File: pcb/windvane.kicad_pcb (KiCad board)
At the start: 2 copper layers, 97.5 x 46 mm, 30 parts, among them J1 Screw_Terminal_01x04, J2 Conn_01x04_Pin, U1 ESP-12F, U2 MCP2515-xSO, U3 AS5600-ASOT, U4 DS18B20, U6 TJA1050, Y1 8MHz

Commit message: place & route
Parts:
- removed C3: 0.1u, Capacitor_SMD:C_0805_2012Metric
- removed H1, H2: MountingHole, MountingHole:MountingHole_2.2mm_M2
- removed J1: Screw_Terminal_01x04, TerminalBlock_Phoenix:TerminalBlock_Phoenix_MKDS-1,5-4-5.08_1x04_P5.08mm_Horizontal
- removed J2: Conn_01x04_Pin, Connector_JST:JST_EH_S4B-EH_1x04_P2.50mm_Horizontal
- removed R3: 10k, Resistor_SMD:R_0805_2012Metric
- removed SS40AF1: ~, Package_TO_SOT_THT:TO-92L_Inline
- added C8: 10u, Capacitor_SMD:C_0805_2012Metric, F.Cu at (139.1, 96.0)
- added J3: Conn_01x08_Socket, Connector_FFC-FPC:Molex_200528-0080_1x08-1MP_P1.00mm_Horizontal, F.Cu at (126.8, 118.3)
- added R11: 10k, Resistor_SMD:R_0805_2012Metric, F.Cu at (134.5, 110.0)
- added U5: ~, Custom:MiniStepDownConverter, F.Cu at (126.1, 103.8)
- added U7: SS40AF1, Package_TO_SOT_THT:TO-92L_Inline, B.Cu at (138.0, 108.6)
- C1, C2: value 22u -> 10u; footprint Capacitor_SMD:C_Elec_5x5.8 -> Capacitor_SMD:C_0805_2012Metric
- C6, C7: value 0.1u -> 10u
- U3: footprint Package_SO:Infineon_PG-DSO-8-43 -> Package_SO:SOIC-8_3.9x4.9mm_P1.27mm
- moved R1 73.3 mm to (159.5, 89.3), turned to -90 degrees
- moved R5 70.6 mm to (155.6, 111.1), turned to 90 degrees
- moved R2 69.4 mm to (155.7, 89.3), turned to -90 degrees
- moved R4 69.3 mm to (153.6, 111.1), turned to 90 degrees
- moved R6 65.9 mm to (151.6, 111.1), turned to 90 degrees
- moved R7 63.0 mm to (149.6, 111.1), turned to 90 degrees
- moved R8 60.1 mm to (147.6, 111.1), turned to -90 degrees
- moved H3 46.2 mm to (153.5, 117.0)
- moved C1 40.8 mm to (134.5, 107.7)
- moved C2 39.3 mm to (145.6, 89.3), turned to -90 degrees
- moved Y1 38.1 mm to (138.5, 90.4), turned to 90 degrees
- moved H4 37.4 mm to (153.7, 85.0)
- moved C4 31.1 mm to (134.5, 86.2), turned to 90 degrees
- moved C5 31.0 mm to (134.5, 89.7), turned to -90 degrees
- moved R10 28.2 mm to (116.9, 87.5)
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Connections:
- C1 pad 1: +12V -> GND
- C1 pad 2: GND -> +12V
- C2 pad 1: +3V3 -> GND
- C2 pad 2: GND -> +3V3
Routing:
- net /MOSI: track 0.00 -> 41.7 mm, vias 0 -> 2
- net Net-(U2-~{RESET}): track 0.00 -> 7.06 mm
- net +3V3: track 0.00 -> 6.25 mm
- net /Speed_Out: track 0.00 -> 5.07 mm
- net Net-(U2-OSC2): track 0.00 -> 4.16 mm
- net Net-(U2-OSC1): track 0.00 -> 4.11 mm
- net +12V: track 0.00 -> 2.96 mm
- net Net-(U1-~{RST}): track 0.00 -> 2.49 mm
- net Net-(U1-EN): track 0.00 -> 2.48 mm
- net /Temp_DQ: track 0.00 -> 2.46 mm
- net Net-(U1-GPIO2): track 0.00 -> 2.34 mm
- net /uC_PRG: track 0.00 -> 2.34 mm
- net /SDA: track 0.00 -> 2.34 mm
- net /SCL: track 0.00 -> 2.34 mm
- net Net-(U1-GPIO15): track 0.00 -> 2.33 mm
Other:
- board size 97.5 x 46 mm -> 60.8 x 40.8 mm

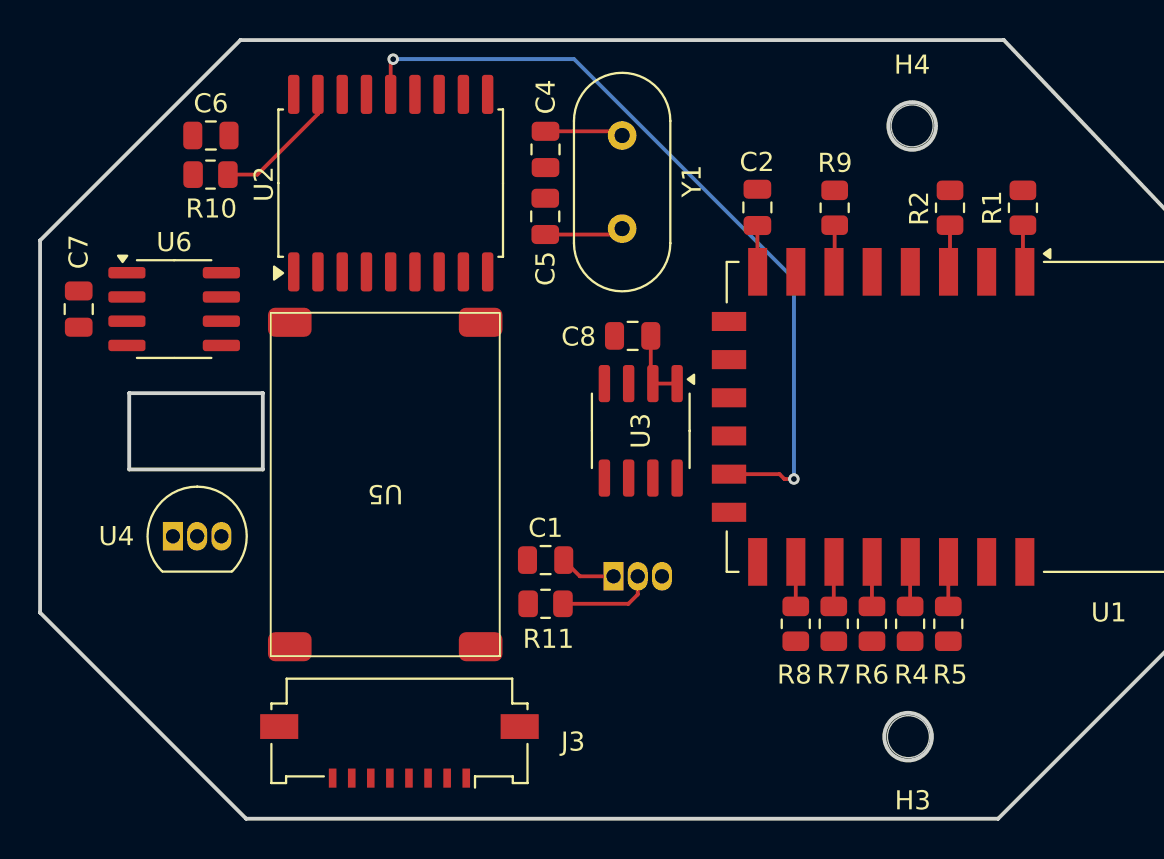
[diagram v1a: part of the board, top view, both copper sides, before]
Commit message: routing - done, next up - review
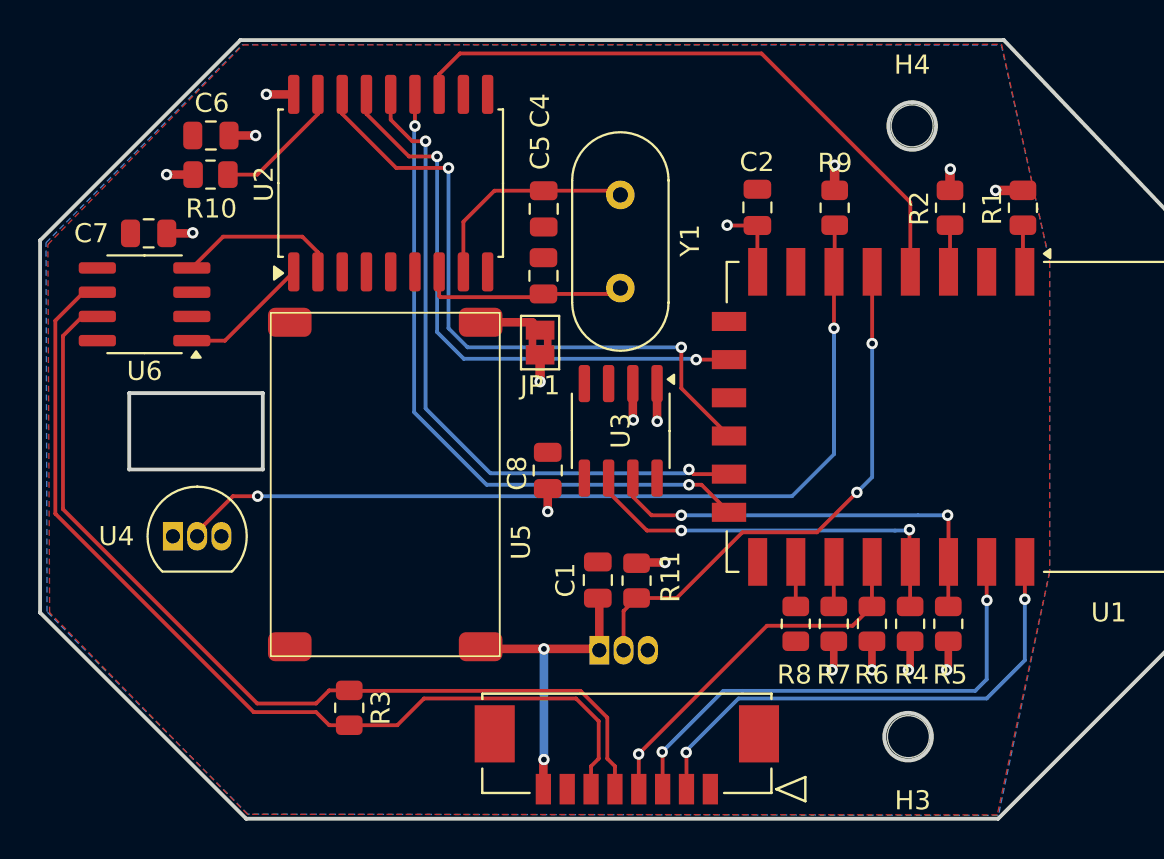
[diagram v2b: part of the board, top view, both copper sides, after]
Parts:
- added JP1: SolderJumper_2_Bridged, Jumper:SolderJumper-2_P1.3mm_Bridged2Bar_Pad1.0x1.5mm, F.Cu at (134.2, 96.3)
- added R3: 120, Resistor_SMD:R_0805_2012Metric, F.Cu at (124.2, 115.5)
- J3: footprint Connector_FFC-FPC:Molex_200528-0080_1x08-1MP_P1.00mm_Horizontal -> Custom:CON_532610871
- moved J3 16.4 mm to (143.1, 119.8)
- moved C8 8.34 mm to (134.6, 103.0), turned to -90 degrees
- moved C7 5.40 mm to (113.7, 90.6), turned to 0 degrees
- moved R11 4.92 mm to (139.3, 108.8), turned to -90 degrees
- moved U7 3.94 mm to (137.3, 112.5)
- moved C4 3.11 mm to (134.4, 89.3)
- moved C5 3.11 mm to (134.4, 92.9)
- moved Y1 3.11 mm to (138.4, 93.5)
- moved C1 2.93 mm to (137.2, 108.8), turned to -90 degrees
- moved U6 1.57 mm to (113.5, 94.3), turned to 180 degrees
- moved U3 1.05 mm to (138.4, 101.0)
- turned U5 to 0 degrees
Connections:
- J3 pad 2: /uC_RXD -> /uC_TXD
- J3 pad 3: /uC_TXD -> /uC_RXD
- J3 pad 5: /CAN_LOW -> /CAN_+
- J3 pad 6: /CAN_HI -> /CAN_-
- U5 pad 3: +3V3 -> Net-(JP1-A)
- U6 pad 6: /CAN_LOW -> /CAN_-
- U6 pad 7: /CAN_HI -> /CAN_+
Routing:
- net /CAN_-: track 0.00 -> 50.8 mm
- net /CAN_+: track 0.00 -> 48.8 mm
- net /Temp_DQ: track 2.46 -> 47.3 mm, vias 0 -> 2
- net /SCLK: track 0.00 -> 35.3 mm, vias 0 -> 2
- net /~{CS}: track 0.00 -> 34.5 mm, vias 0 -> 2
- net /CAN_~{Int}: track 0.00 -> 33.1 mm
- net /MISO: track 0.00 -> 30.7 mm, vias 0 -> 2
- net /uC_TXD: track 0.00 -> 26.9 mm, vias 0 -> 2
- net /uC_RXD: track 0.00 -> 26.7 mm, vias 0 -> 2
- net /Speed_Out: track 5.07 -> 28.7 mm, vias 0 -> 2
- net +3V3: track 6.25 -> 27.5 mm, vias 0 -> 17
- net /SCL: track 2.34 -> 22.7 mm, vias 0 -> 2
- net /SDA: track 2.34 -> 22.2 mm, vias 0 -> 2
- net /uC_PRG: track 2.34 -> 19.7 mm, vias 0 -> 1
- net +12V: track 2.96 -> 16.6 mm, vias 0 -> 2
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- added copper zone on B.Cu, net +3V3
- added copper zone on F.Cu, net GND

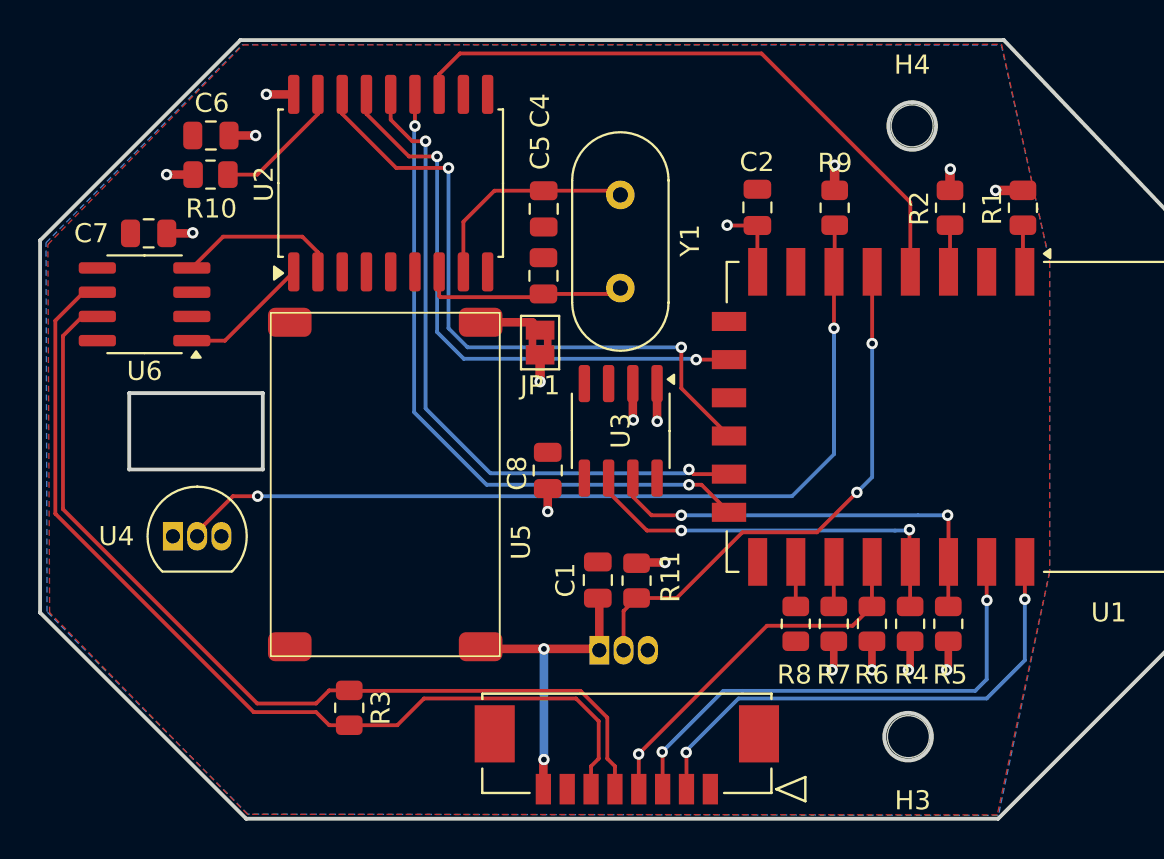
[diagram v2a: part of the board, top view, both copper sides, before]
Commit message: bugfixing: connected esp reset to connector, corrected wrong pin assigment of RPM sensor, improved routing, remapped CAN interrupt to GPIO9
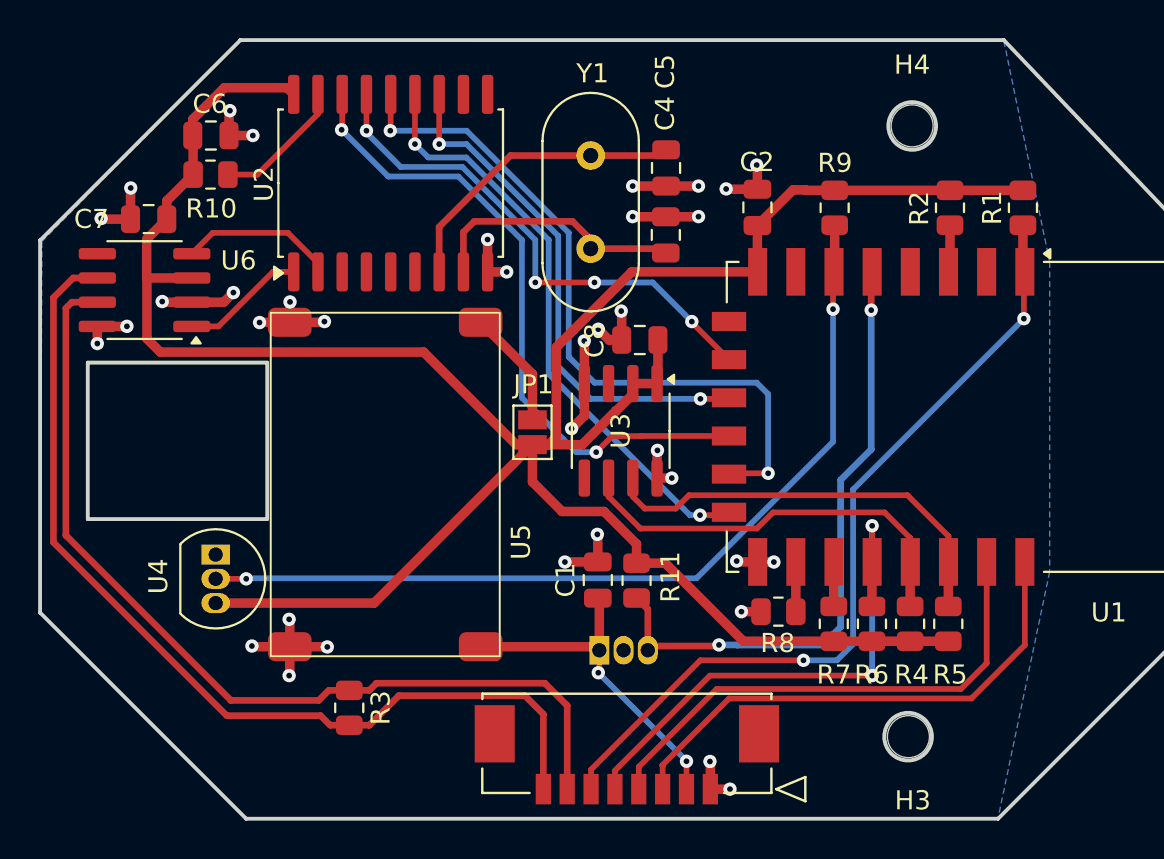
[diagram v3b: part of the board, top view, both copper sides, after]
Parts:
- JP1: value SolderJumper_2_Bridged -> SolderJumper_2_Open; footprint Jumper:SolderJumper-2_P1.3mm_Bridged2Bar_Pad1.0x1.5mm -> Jumper:SolderJumper-2_P1.3mm_Open_Pad1.0x1.5mm
- moved C5 8.56 mm to (140.8, 87.2), turned to 90 degrees
- moved C8 8.36 mm to (139.4, 96.2), turned to 0 degrees
- moved Y1 7.12 mm to (136.8, 86.5), turned to -90 degrees
- moved C4 6.54 mm to (140.8, 90.7), turned to -90 degrees
- moved JP1 4.72 mm to (133.8, 101.0)
- moved U4 2.44 mm to (117.2, 107.5), turned to -90 degrees
- moved R8 1.11 mm to (146.7, 110.5), turned to 180 degrees
- moved C7 0.75 mm to (113.7, 89.9)
- moved U6 0.75 mm to (113.5, 93.6)
- turned C6 to 180 degrees
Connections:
- J3 pad 2: /uC_TXD -> +12V
- J3 pad 3: /uC_RXD -> /uC_TXD
- J3 pad 4: /uC_PRG -> /uC_RXD
- J3 pad 5: /CAN_+ -> /uC_PRG
- J3 pad 6: /CAN_- -> /~{RST}
- J3 pad 7: unconnected-(J3-Pin_7-Pad7) -> /CAN_+
- J3 pad 8: +12V -> /CAN_-
- R1 pad 2: Net-(U1-~{RST}) -> /~{RST}
- U1 pad 1: Net-(U1-~{RST}) -> /~{RST}
- U1 pad 11: unconnected-(U1-GPIO9-Pad11) -> /CAN_~{Int}
- U1 pad 4: /CAN_~{Int} -> unconnected-(U1-GPIO16-Pad4)
- U7 pad 2: /Speed_Out -> GND
- U7 pad 3: GND -> /Speed_Out
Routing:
- net +3V3: track 27.5 -> 137.2 mm, vias 17 -> 0
- net GND: track 0.00 -> 55.1 mm, vias 0 -> 36
- net /~{RST}: track 0.00 -> 43.2 mm, vias 0 -> 2
- net /uC_PRG: track 19.7 -> 28.6 mm, vias 1 -> 2
- net /CAN_~{Int}: track 33.1 -> 27.4 mm, vias 0 -> 2
- net Net-(U2-OSC2): track 11.0 -> 15.9 mm
- net /Speed_Out: track 28.7 -> 33.3 mm
- net /SCLK: track 35.3 -> 31.3 mm
- net /MISO: track 30.7 -> 27.3 mm, vias 2 -> 4
- net Net-(JP1-A): track 3.29 -> 6.24 mm
- net Net-(U1-~{RST}): track 2.49 -> 0.00 mm
- net /MOSI: track 35.1 -> 37.5 mm
- net Net-(U2-OSC1): track 11.6 -> 13.9 mm
- net +12V: track 16.6 -> 18.3 mm
- net /CAN_-: track 50.8 -> 50.2 mm
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- added copper zone on B.Cu, net GND
- removed copper zone on B.Cu, net +3V3
- removed copper zone on F.Cu, net GND
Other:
- outline, holes or cut-outs redrawn
